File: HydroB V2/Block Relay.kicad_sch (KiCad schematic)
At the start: 25 parts, among them J14 Screw_Terminal_01x02, J15 Screw_Terminal_01x02, J16 Screw_Terminal_01x02, J17 Screw_Terminal_01x02, J18 Screw_Terminal_01x02, K10 SRD-05VDC-SL-C, K5 SRD-05VDC-SL-C, K7 SRD-05VDC-SL-C, K8 SRD-05VDC-SL-C, K9 SRD-05VDC-SL-C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

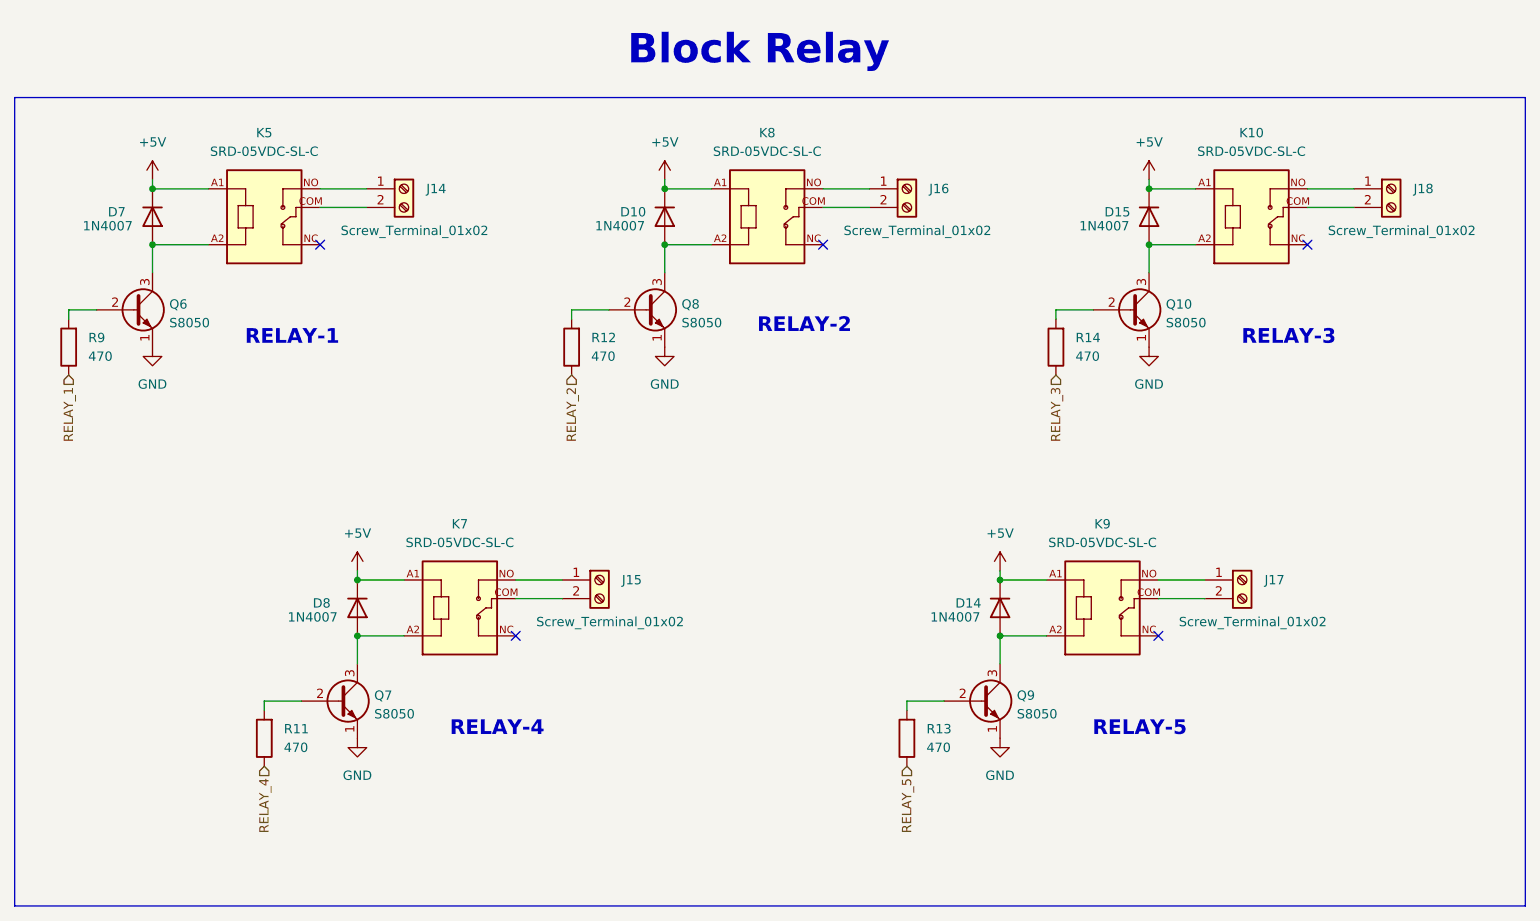
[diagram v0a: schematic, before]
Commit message: Update power supply and connector of sensor
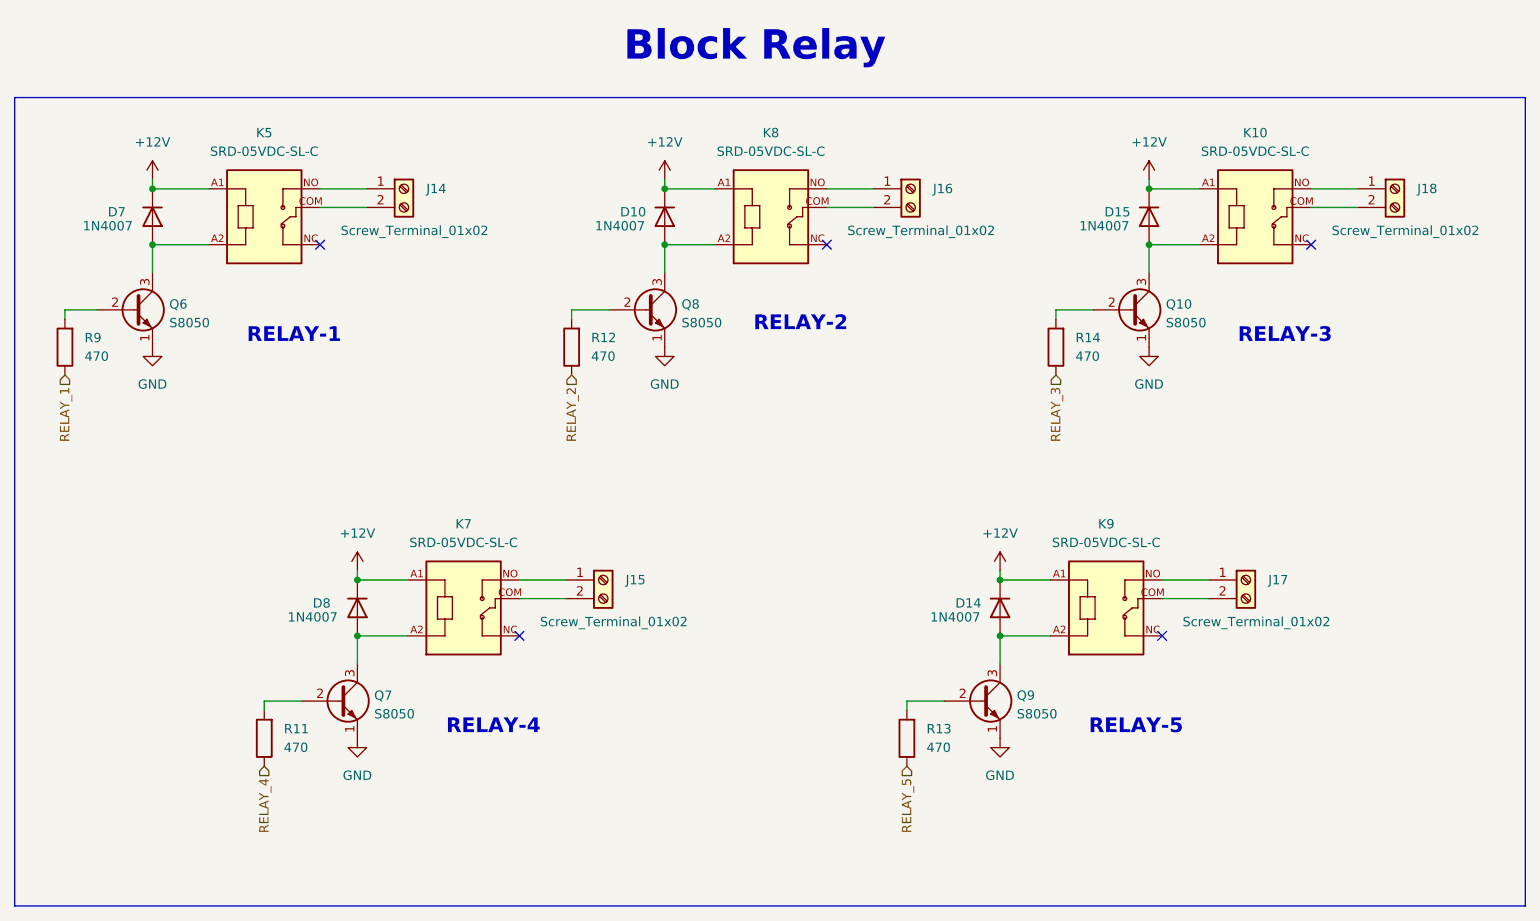
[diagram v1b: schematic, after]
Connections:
- net +5V renamed +12V
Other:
- moved on the sheet: J15, J16, J17, J18, K10, K7, K8, K9, R9
